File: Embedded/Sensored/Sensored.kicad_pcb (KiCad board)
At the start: 2 copper layers, 15 x 15 mm, 23 parts, among them J1 SDA, J10 SCL, J2 PWR, J3 GND, J4 PWR, J5 GND, J6 PWR, J7 GND, J8 PWR, J9 GND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

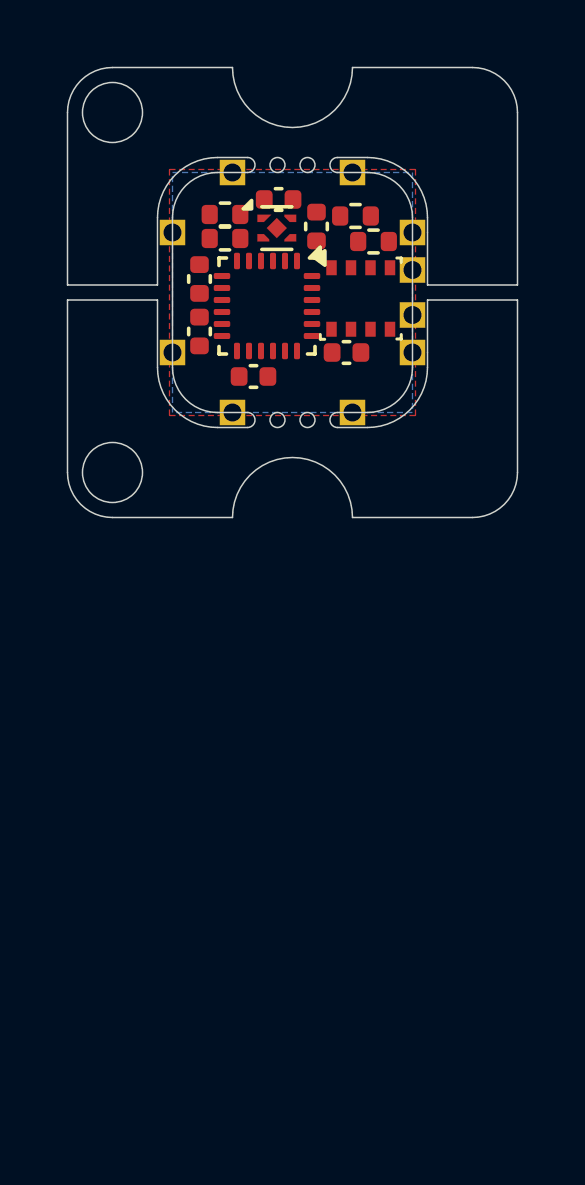
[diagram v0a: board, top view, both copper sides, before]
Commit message: Modified Component Placement & Added Adapting Pads
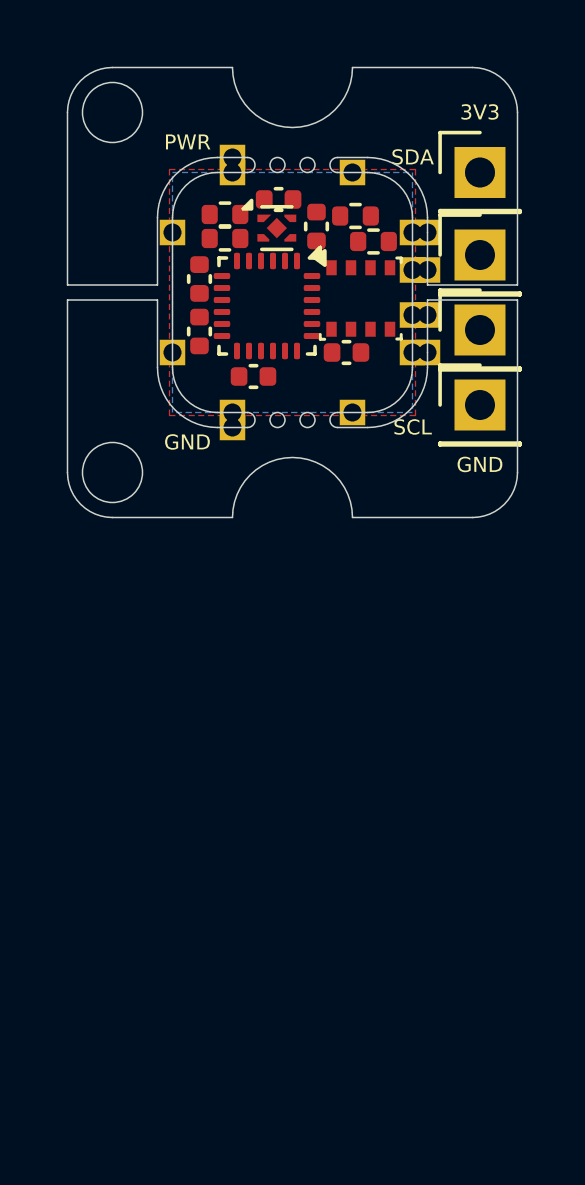
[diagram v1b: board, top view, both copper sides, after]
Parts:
- added J11: SDA, Custom Connectors:1mm Pads, F.Cu at (79.5, 39.2)
- added J12: SCL, Custom Connectors:1mm Pads, F.Cu at (79.5, 40.8)
- added J13: PWR, Custom Connectors:1mm Pads, F.Cu at (79.5, 38.0)
- added J14: GND, Custom Connectors:1mm Pads, F.Cu at (79.5, 42.0)
- added J15: PWR, Custom Connectors:1mm Pads, F.Cu at (73.0, 35.5)
- added J16: GND, Custom Connectors:1mm Pads, F.Cu at (73.0, 44.5)
- added TP1: 3V3, Connector_PinHeader_2.54mm:PinHeader_1x01_P2.54mm_Vertical, F.Cu at (81.2, 36.0)
- added TP2: SDA, Connector_PinHeader_2.54mm:PinHeader_1x01_P2.54mm_Vertical, F.Cu at (81.2, 38.8)
- added TP3: SCL, Connector_PinHeader_2.54mm:PinHeader_1x01_P2.54mm_Vertical, F.Cu at (81.2, 41.2)
- added TP4: GND, Connector_PinHeader_2.54mm:PinHeader_1x01_P2.54mm_Vertical, F.Cu at (81.2, 43.8)

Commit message: Added Component Routing
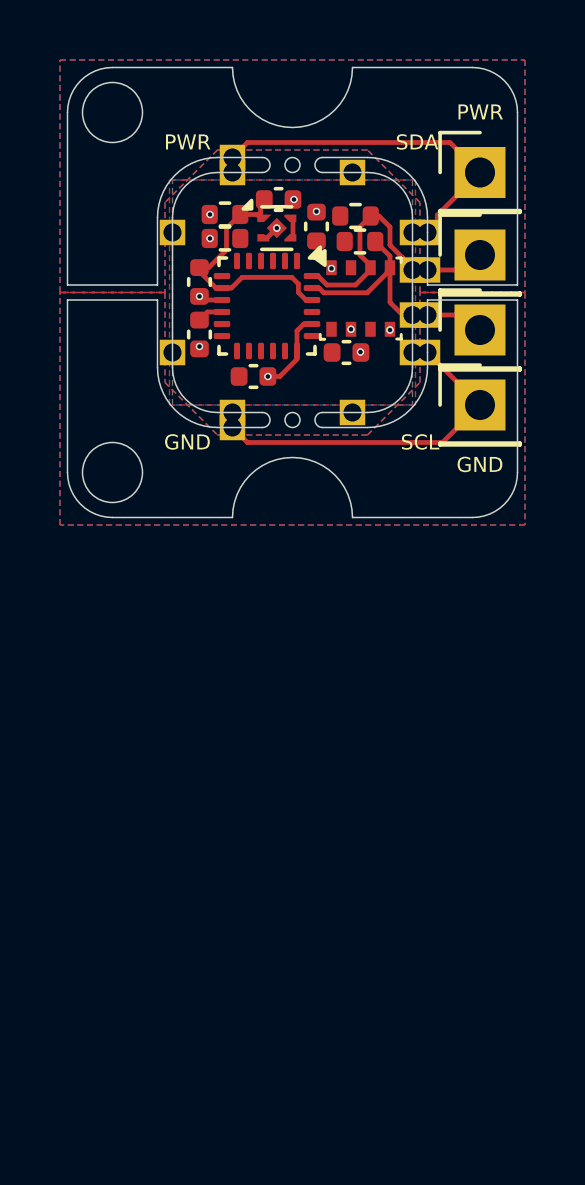
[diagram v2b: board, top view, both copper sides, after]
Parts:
- TP1: value 3V3 -> PWR
- moved R1 0.45 mm to (77.2, 38.3)
- moved C1 0.10 mm to (71.9, 39.6), turned to 90 degrees
- moved C4 0.10 mm to (71.9, 41.4)
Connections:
- net Net-(J13-Pin_1) renamed +3V3E
- net Net-(J14-Pin_1) renamed GNDE
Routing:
- net +3V3E: track 0.00 -> 11.5 mm
- net GNDE: track 0.00 -> 11.3 mm
- net +1V8: track 0.00 -> 8.68 mm
- net SDA: track 0.00 -> 6.54 mm
- net SCL: track 0.00 -> 5.94 mm
- net GND: track 0.00 -> 4.39 mm, vias 0 -> 12
- net Net-(J12-Pin_1): track 0.00 -> 1.63 mm
- net Net-(J11-Pin_1): track 0.00 -> 1.63 mm
- net Net-(U1-REGOUT): track 0.00 -> 0.86 mm
- net +3V3: track 0.00 -> 0.65 mm
- added copper zone on B.Cu, net +3V3E
- added copper zone on F.Cu, net +3V3E
- added copper zone on B.Cu, net GNDE
- added copper zone on F.Cu, net GNDE
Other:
- outline, holes or cut-outs redrawn

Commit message: Added Orientation Marker
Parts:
- added G***: LOGO, LOGO, F.Cu at (69.2, 38.0)
- added G***: LOGO, LOGO, B.Cu at (73.3, 40.0)
- J13, J15, J2, J4, J6, J8, TP1: value PWR -> 3V3
- U1: footprint Sensor_Motion:InvenSense_QFN-24_3x3mm_P0.4mm -> Sensor_Motion:InvenSense_QFN-24_3x3mm_P0.4mm_NoMask
- moved TP1 0.25 mm to (81.2, 36.2)
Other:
- board text added: "x"
- board text added: "y"
- board text added: "z"

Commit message: Verified LCSC Components
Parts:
- U1: footprint Sensor_Motion:InvenSense_QFN-24_3x3mm_P0.4mm_NoMask -> Sensor_Motion:InvenSense_QFN-24_3x3mm_P0.4mm
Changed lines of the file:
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@@
 		)
 	)
-	(footprint "Sensor_Motion:InvenSense_QFN-24_3x3mm_P0.4mm_NoMask"
+	(footprint "Sensor_Motion:InvenSense_QFN-24_3x3mm_P0.4mm"
 		(layer "F.Cu")
 		(at 74.15 40.45 -90)
-		(descr "24-Lead Plastic QFN (3mm x 3mm); Pitch 0.4mm; EP 1.7x1.54mm; for InvenSense motion sensors; Mask removed below exposed pad; keepout area marked (Package see: https://store.invensense.com/datasheets/invensense/MPU9250REV1.0.pdf; See also https://www.invensense.com/wp-content/uploads/2015/02/InvenSense-MEMS-Handling.pdf)")
+		(descr "24-Lead Plastic QFN (3mm x 3mm); Pitch 0.4mm; EP 1.7x1.54mm; for InvenSense motion sensors; keepout area marked (Package see: https://store.invensense.com/datasheets/invensense/MPU9250REV1.0.pdf; See also https://www.invensense.com/wp-content/uploads/2015/02/InvenSense-MEMS-Handling.pdf)")
 		(tags "QFN 0.4")
 		(property "Reference" "U1"
 			(at 0 -3.25 90)
 			(layer "F.SilkS")
+			(hide yes)
 			(effects
 				(font
@@
 			)
 		)
-		(property "Footprint" "Sensor_Motion:InvenSense_QFN-24_3x3mm_P0.4mm_NoMask"
+		(property "Footprint" "Sensor_Motion:InvenSense_QFN-24_3x3mm_P0.4mm"
 			(at 0 0 -90)
 			(unlocked yes)
@@
 			(layer "F.Fab")
 		)
+		(fp_text user "KEEPOUT"
+			(at 0 -0.5 90)
+			(layer "Cmts.User")
+			(effects
+				(font
+					(size 0.2 0.2)
+					(thickness 0.04)
+				)
+			)
+		)
 		(fp_text user "Component"
 			(at 0 0.55 90)
@@
 			)
 		)
-		(fp_text user "KEEPOUT"
-			(at 0 -0.5 90)
-			(layer "Cmts.User")
-			(effects
-				(font
-					(size 0.2 0.2)
-					(thickness 0.04)
-				)
-			)
-		)
 		(fp_text user "No Copper"
 			(at 0 -0.1 90)
@@
 				)
 			)
-		)
-		(pad "" smd roundrect
-			(at 0 0 270)
-			(size 1.75 1.59)
-			(layers "F.Mask")
-			(roundrect_rratio 0.15)
 		)
 		(pad "1" smd roundrect
@@
 	(via
 		(at 75.8 37.3)
-		(size 0.25)
-		(drill 0.15)
+		(size 0.4)
+		(drill 0.3)
 		(layers "F.Cu" "B.Cu")
 		(net 1)
@@
 	(via
 		(at 75.05 36.9)
-		(size 0.25)
-		(drill 0.15)
+		(size 0.4)
+		(drill 0.3)
 		(layers "F.Cu" "B.Cu")
 		(net 1)
@@
 	(via
 		(at 74.4775 37.852501)
-		(size 0.25)
-		(drill 0.15)
+		(size 0.4)
+		(drill 0.3)
 		(layers "F.Cu" "B.Cu")
 		(net 1)
@@
 	(via
 		(at 76.3 39.2)
-		(size 0.25)
-		(drill 0.15)
+		(size 0.4)
+		(drill 0.3)
 		(layers "F.Cu" "B.Cu")
 		(net 1)
@@
 	(via
 		(at 74.18 42.800001)
-		(size 0.25)
-		(drill 0.15)
+		(size 0.4)
+		(drill 0.3)
 		(layers "F.Cu" "B.Cu")
 		(net 1)
@@
 	(via
 		(at 77.265 41.985)
-		(size 0.25)
-		(drill 0.15)
+		(size 0.4)
+		(drill 0.3)
 		(layers "F.Cu" "B.Cu")
 		(net 1)
@@
 	(via
 		(at 71.9 41.8)
-		(size 0.25)
-		(drill 0.15)
+		(size 0.4)
+		(drill 0.3)
 		(layers "F.Cu" "B.Cu")
 		(net 1)
@@
 	(via
 		(at 72.25 37.4)
-		(size 0.25)
-		(drill 0.15)
+		(size 0.4)
+		(drill 0.3)
 		(layers "F.Cu" "B.Cu")
 		(net 1)
@@
 	(via
 		(at 72.25 38.2)
-		(size 0.25)
-		(drill 0.15)
+		(size 0.4)
+		(drill 0.3)
 		(layers "F.Cu" "B.Cu")
 		(net 1)
@@
 	(via
 		(at 71.9 40.13)
-		(size 0.25)
-		(drill 0.15)
+		(size 0.4)
+		(drill 0.3)
 		(layers "F.Cu" "B.Cu")
 		(net 1)
@@
 	(via
 		(at 76.95 41.225)
-		(size 0.25)
-		(drill 0.15)
+		(size 0.4)
+		(drill 0.3)
 		(layers "F.Cu" "B.Cu")
 		(net 1)
@@
 	(via
 		(at 78.25 41.25)
-		(size 0.25)
-		(drill 0.15)
+		(size 0.4)
+		(drill 0.3)
 		(layers "F.Cu" "B.Cu")
 		(net 1)

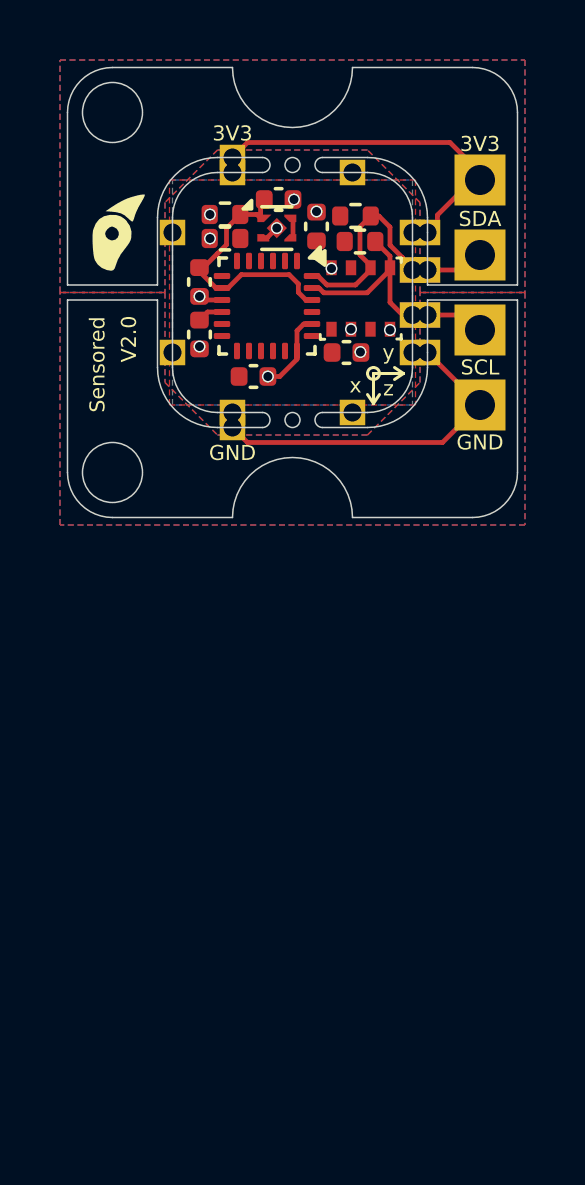
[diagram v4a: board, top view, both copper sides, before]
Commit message: Modified Layout for JLCPCB
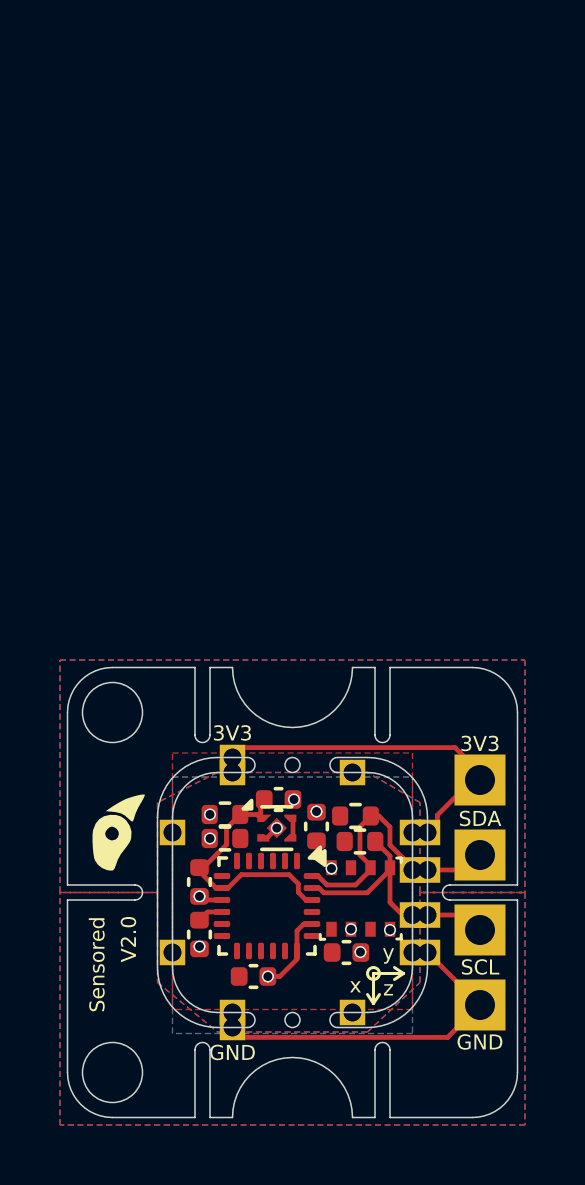
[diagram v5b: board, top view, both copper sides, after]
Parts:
- moved C1 20.0 mm to (71.9, 59.6)
- moved C11 20.0 mm to (72.8, 57.4)
- moved C13 20.0 mm to (74.5, 56.9)
- moved C3 20.0 mm to (73.7, 62.8)
- moved C4 20.0 mm to (71.9, 61.4)
- moved C6 20.0 mm to (75.8, 57.8)
- moved C8 20.0 mm to (76.8, 62.0)
- moved C9 20.0 mm to (72.8, 58.2)
- moved G*** 20.0 mm to (69.2, 58.0)
- moved G*** 20.0 mm to (73.3, 60.0)
- moved J1 20.0 mm to (79.0, 59.2)
- moved J10 20.0 mm to (79.0, 60.8)
- moved J11 20.0 mm to (79.5, 59.2)
- moved J12 20.0 mm to (79.5, 60.8)
- moved J13 20.0 mm to (79.5, 58.0)
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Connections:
- J13 pad 1: +3V3E -> +3V3
- J14 pad 1: GNDE -> GND
- J15 pad 1: +3V3E -> +3V3
- J16 pad 1: GNDE -> GND
- TP1 pad 1: +3V3E -> +3V3
- TP4 pad 1: GNDE -> GND
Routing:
- net +3V3E: track 11.5 -> 0.00 mm
- net +3V3: track 0.65 -> 12.0 mm
- net GNDE: track 11.3 -> 0.00 mm
- net GND: track 4.39 -> 15.6 mm
- added copper zone on B.Cu, net +3V3
- added copper zone on F.Cu, net GND
- removed copper zone on B.Cu, net +3V3E
- removed copper zone on F.Cu, net +3V3E
- removed copper zone on B.Cu, net GNDE
- removed copper zone on F.Cu, net GNDE
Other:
- outline, holes or cut-outs redrawn
